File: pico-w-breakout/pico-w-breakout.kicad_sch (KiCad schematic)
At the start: 6 parts, among them J1 Conn_01x20, J2 Conn_01x20, J3 Conn_01x20, J4 Conn_01x20, J5 Conn_01x03, J6 Conn_01x03

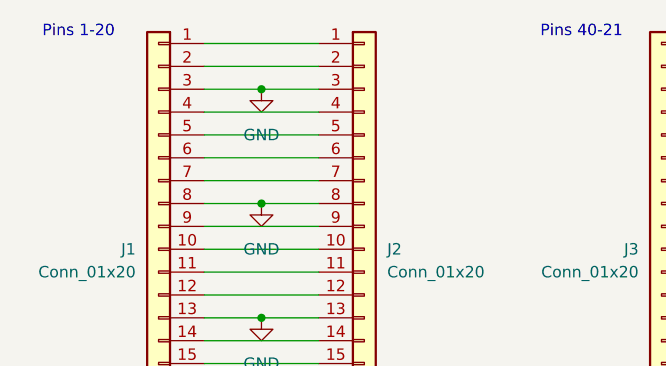
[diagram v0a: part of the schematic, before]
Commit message: Add series resistor to GPIO 2
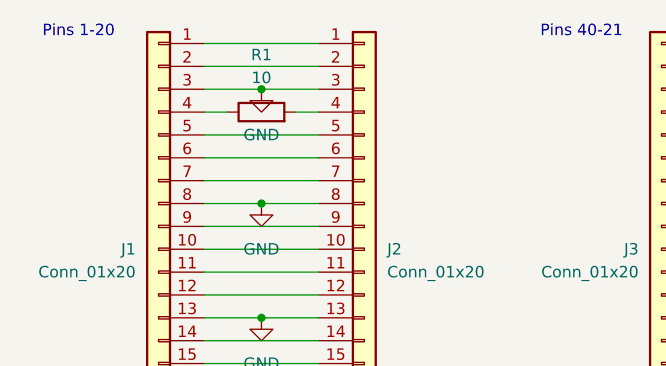
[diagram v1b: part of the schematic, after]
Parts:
- added R1: 10, Resistor_SMD:R_0603_1608Metric, symbol Device:R
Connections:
- net at J1.4 (Pin_4): now also R1.1; no longer J2.4 (Pin_4)
- new net: J2.4 (Pin_4), R1.2
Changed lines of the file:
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@@
+	(wire
+		(pts
+			(xy 35.56 27.94) (xy 38.1 27.94)
+		)
+		(stroke
+			(width 0)
+			(type default)
+		)
+	)
 	(wire
 		(pts
@@
 	(wire
 		(pts
+			(xy 45.72 27.94) (xy 48.26 27.94)
+		)
+		(stroke
+			(width 0)
+			(type default)
+		)
+	)
+	(wire
+		(pts
 			(xy 41.91 63.5) (xy 48.26 63.5)
 		)
@@
 		(pts
 			(xy 91.44 22.86) (xy 104.14 22.86)
-		)
-		(stroke
-			(width 0)
-			(type default)
-		)
-	)
-	(wire
-		(pts
-			(xy 35.56 27.94) (xy 48.26 27.94)
 		)
 		(stroke
@@
 			)
 		)
+	)
+	(symbol
+		(lib_id "Device:R")
+		(at 41.91 27.94 90)
+		(unit 1)
+		(exclude_from_sim no)
+		(in_bom yes)
+		(on_board yes)
+		(dnp no)
+		(fields_autoplaced yes)
+		(property "Reference" "R1"
+			(at 41.91 21.59 90)
+			(effects
+				(font
+					(size 1.27 1.27)
+				)
+			)
+		)
+		(property "Value" "10"
+			(at 41.91 24.13 90)
+			(effects
+				(font
+					(size 1.27 1.27)
+				)
+			)
+		)
+		(property "Footprint" "Resistor_SMD:R_0603_1608Metric"
+			(at 41.91 29.718 90)
+			(effects
+				(font
+					(size 1.27 1.27)
+				)
+				(hide yes)
+			)
+		)
+		(property "Datasheet" "~"
+			(at 41.91 27.94 0)
+			(effects
+				(font
+					(size 1.27 1.27)
+				)
+				(hide yes)
+			)
+		)
+		(property "Description" "Resistor"
+			(at 41.91 27.94 0)
+			(effects
+				(font
+					(size 1.27 1.27)
+				)
+				(hide yes)
+			)
+		)
+		(pin "2"
+		)
+		(pin "1"
+		)
+		(instances
+			(project ""
+				(path "/18c791f4-e940-4e36-b51d-61b81c54794f"
+					(reference "R1")
+					(unit 1)
+				)
+			)
+		)
